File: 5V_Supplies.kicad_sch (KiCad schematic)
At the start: 22 parts, among them U1401 ADP2370, U1402 uA7805

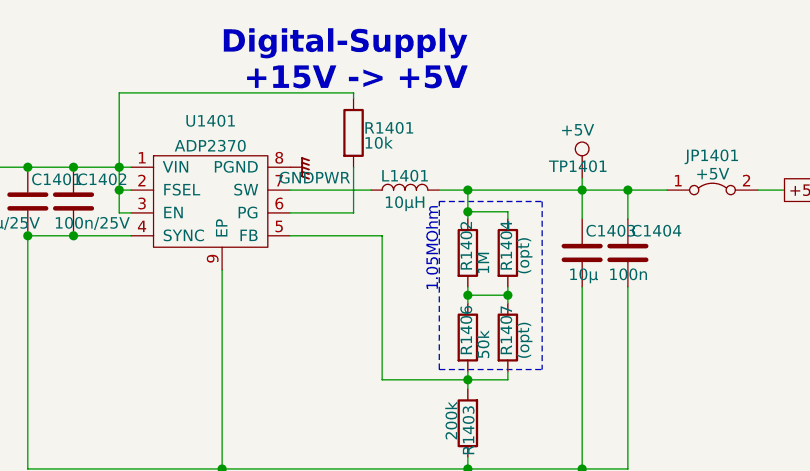
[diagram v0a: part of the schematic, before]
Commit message: FEAR-16 V2.2
PCB-Changes:
 - Added rudimentary "load-balancer" (not really a balancer, but should avoid the DC/DC from regulating against each other!)
 - Added optional GND-jumpers to the N/C pins of the shields
 - Modified amplification adjustment:
   -> Added a offset resistor in row to the trim-poti for amplification for finer amp-tuning
   -> Reduced trim-poti-value from 1Meg -> 50k (20x finer adjustment-range)
      Poti can in the range of:
      - 30k (min) for being able to reach the correct amplification
      - 50k (max) for having at least 20x finer tune-range and a bit of reserve, as 30k is pretty thight on tolerance

Misc.:
 - Added LICENSE.md
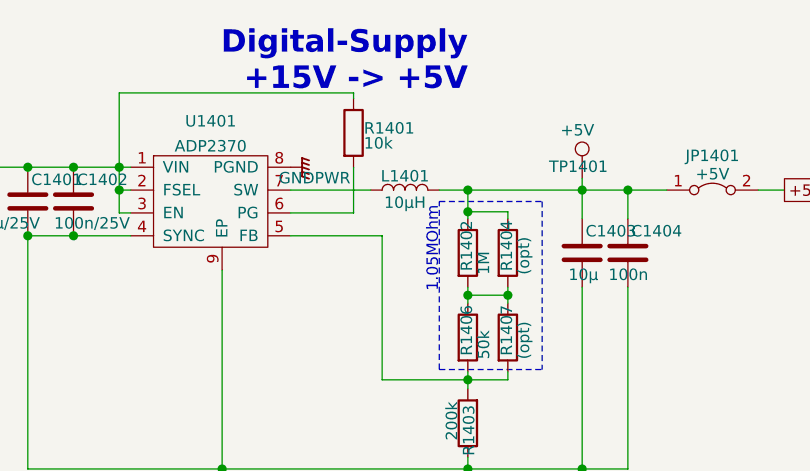
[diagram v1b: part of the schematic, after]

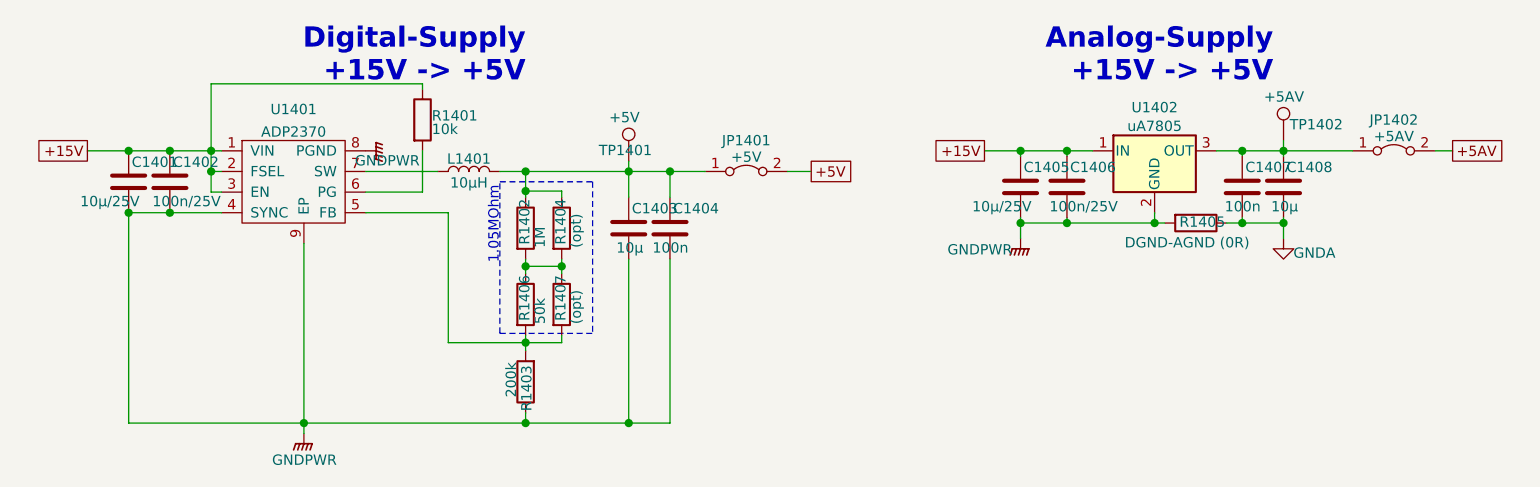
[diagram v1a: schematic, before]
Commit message: Fixed ADP2370 designator
ADP2370 has a bunch of fixed output voltages and an adjustable model.
We use the adjustable model, so we fixed the name matching with the correct model-name.
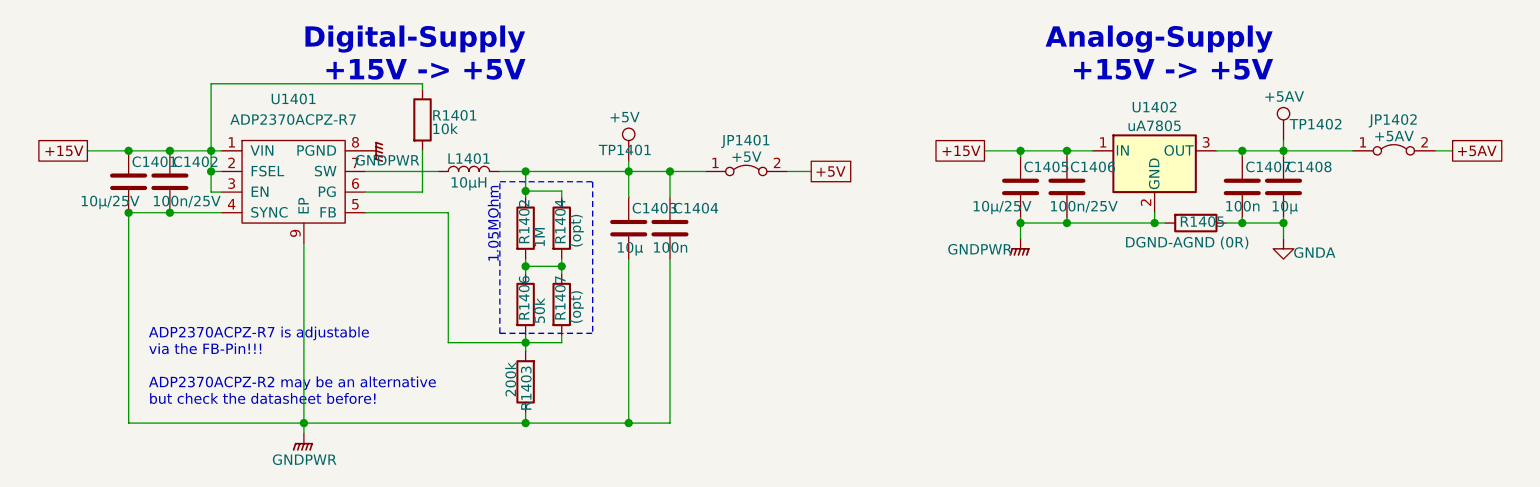
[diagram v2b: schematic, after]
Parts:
- U1401: value ADP2370 -> ADP2370ACPZ-R7
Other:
- note added: "ADP2370ACPZ-R7 is adjustable via the FB-Pin!!! ADP2370ACPZ-R2 may be an alternative but check the datasheet before!"

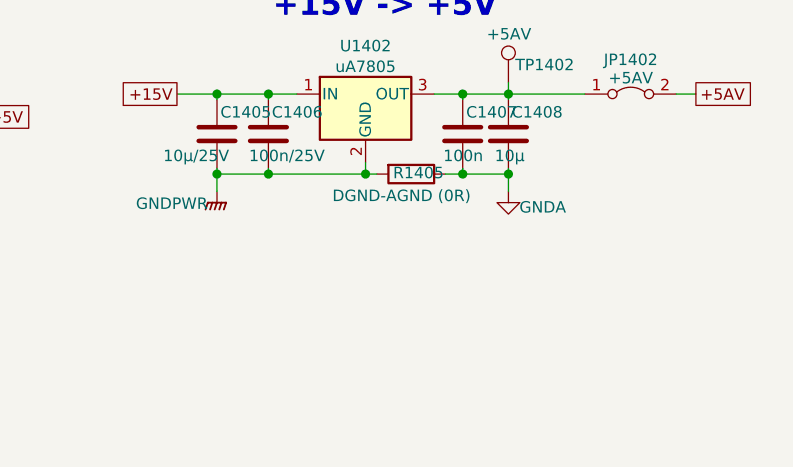
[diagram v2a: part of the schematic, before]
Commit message: Finished README.md
- Adjustment in .gitignore
- Finished first README.md attempt
- Added extra comments to "5V_Supplies"
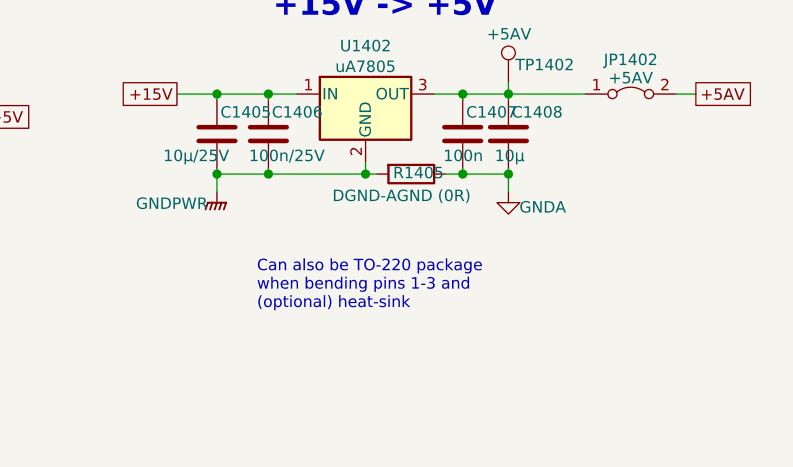
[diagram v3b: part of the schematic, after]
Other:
- note added: "Can also be TO-220 package when bending pins 1-3 and (optional) heat-sink"
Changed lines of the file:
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@@
+		)
+	)
+	(text "Can also be TO-220 package\nwhen bending pins 1-3 and\n(optional) heat-sink"
+		(exclude_from_sim no)
+		(at 149.86 61.92 0)
+		(effects
+			(font
+				(size 1.27 1.27)
+			)
+			(justify left)
 		)
 	)
